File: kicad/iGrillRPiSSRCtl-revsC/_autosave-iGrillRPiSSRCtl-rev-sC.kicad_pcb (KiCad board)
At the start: 2 copper layers, 65 x 56 mm, 21 parts, among them J1 Conn_01x02, P1 Conn_02x20_Odd_Even

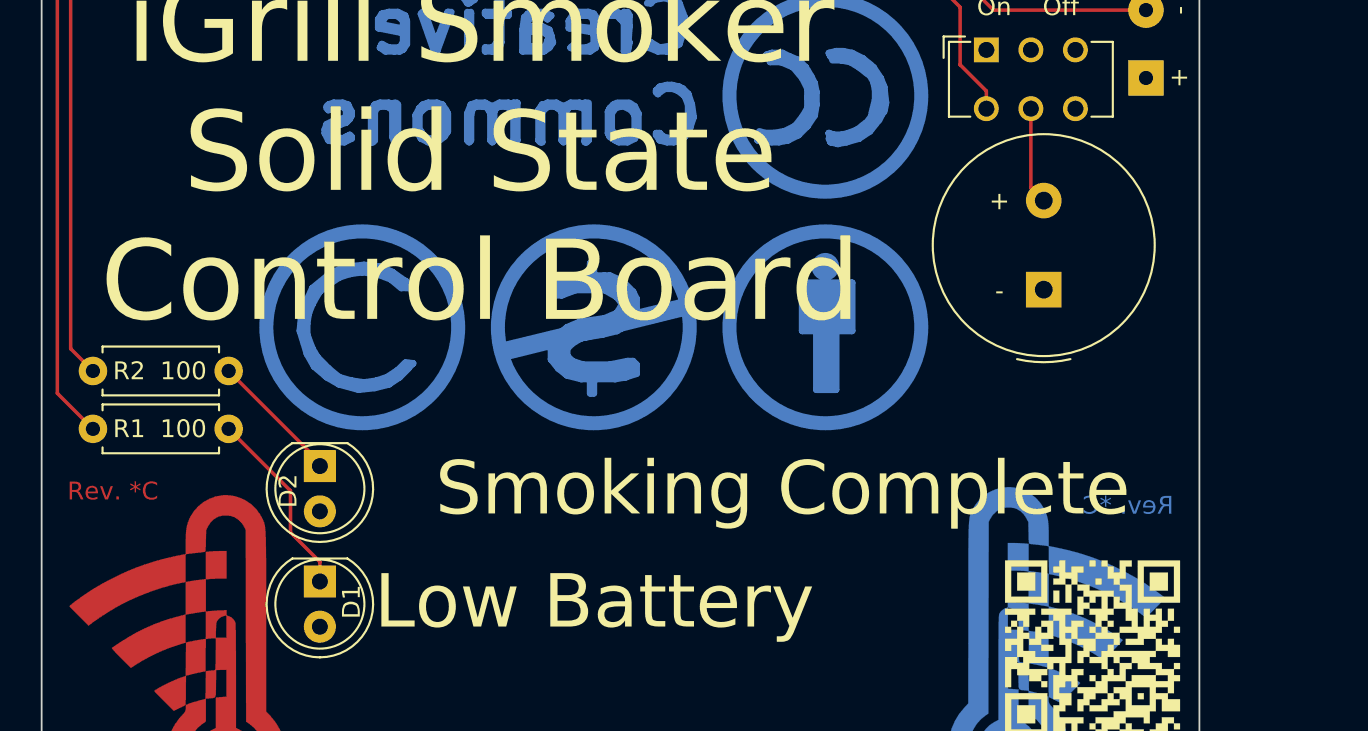
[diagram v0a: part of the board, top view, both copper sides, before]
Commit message: Electrical Cleanup of Schematic
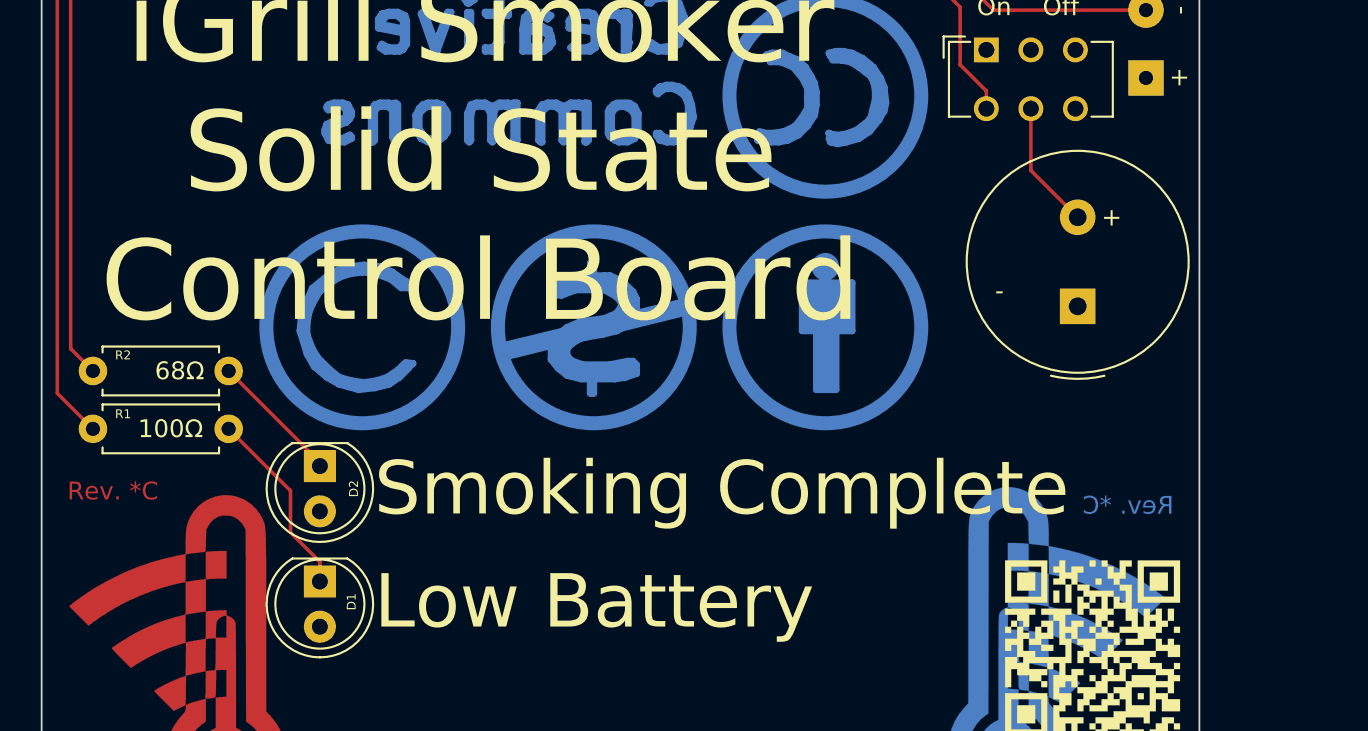
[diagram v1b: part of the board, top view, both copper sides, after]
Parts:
- R1: value 100 -> 100Ω
- R2: value 100 -> 68Ω
- moved BZ1 2.12 mm to (75.3, 43.6)
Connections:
- On    Off pad 6: Net-(SW1-Pad6) -> +5V
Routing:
- net Net-(BZ1-Pad2): track 5.46 -> 7.19 mm
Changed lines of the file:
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@@
     (zones 0)
     (modules 21)
-    (nets 25)
+    (nets 24)
   )
   (page A3)
@@
   (net 22 "Net-(D2-Pad1)")
   (net 23 "Net-(BZ1-Pad2)")
-  (net 24 "Net-(SW1-Pad6)")
   (net_class Default "This is the default net class."
     (clearance 0.2)
@@
     (add_net "Net-(D1-Pad1)")
     (add_net "Net-(D2-Pad1)")
-    (add_net "Net-(SW1-Pad6)")
   )
   (net_class Power ""
@@
     (fp_line (start -1 -0.35) (end -2 0.65) (layer F.Fab) (width 0.1))
     (pad 6 thru_hole circle (at 5 3.3) (size 1.4 1.4) (drill 0.9) (layers *.Cu *.Mask)
-      (net 24 "Net-(SW1-Pad6)"))
+      (net 2 +5V))
     (pad 5 thru_hole circle (at 2.5 3.3) (size 1.4 1.4) (drill 0.9) (layers *.Cu *.Mask)
       (net 23 "Net-(BZ1-Pad2)"))
@@
     (descr "Resistor, Axial_DIN0207 series, Axial, Horizontal, pin pitch=7.62mm, 0.25W = 1/4W, length*diameter=6.3*2.5mm^2, http://cdn-reichelt.de/documents/datenblatt/B400/1_4W%23YAG.pdf")
     (tags "Resistor Axial_DIN0207 series Axial Horizontal pin pitch 7.62mm 0.25W = 1/4W length 6.3mm diameter 2.5mm")
-    (fp_text reference R2 (at 2.032 0) (layer F.SilkS)
-      (effects (font (size 1 1) (thickness 0.15)))
-    )
-    (fp_text value 100 (at 5.08 0) (layer F.SilkS)
+    (fp_text reference R2 (at 1.692 -0.882) (layer F.SilkS)
+      (effects (font (size 0.5 0.5) (thickness 0.075)))
+    )
+    (fp_text value 68Ω (at 4.867 0) (layer F.SilkS)
       (effects (font (size 1 1) (thickness 0.15)))
     )
@@
     (descr "Resistor, Axial_DIN0207 series, Axial, Horizontal, pin pitch=7.62mm, 0.25W = 1/4W, length*diameter=6.3*2.5mm^2, http://cdn-reichelt.de/documents/datenblatt/B400/1_4W%23YAG.pdf")
     (tags "Resistor Axial_DIN0207 series Axial Horizontal pin pitch 7.62mm 0.25W = 1/4W length 6.3mm diameter 2.5mm")
-    (fp_text reference R1 (at 2.032 0) (layer F.SilkS)
-      (effects (font (size 1 1) (thickness 0.15)))
-    )
-    (fp_text value 100 (at 5.08 0) (layer F.SilkS)
+    (fp_text reference R1 (at 1.692 -0.83) (layer F.SilkS)
+      (effects (font (size 0.5 0.5) (thickness 0.075)))
+    )
+    (fp_text value 100Ω (at 4.359 0) (layer F.SilkS)
       (effects (font (size 1 1) (thickness 0.15)))
     )
@@
     (descr "LED, diameter 5.0mm, 2 pins, http://cdn-reichelt.de/documents/datenblatt/A500/LL-504BC2E-009.pdf")
     (tags "LED diameter 5.0mm 2 pins")
-    (fp_text reference D2 (at 1.397 1.778 90) (layer F.SilkS)
-      (effects (font (size 1 1) (thickness 0.15)))
-    )
-    (fp_text value "Smoking Complete" (at 1.27 -45.5 180) (layer F.SilkS)
-      (effects (font (size 3 3) (thickness 0.45)) (justify right))
+    (fp_text reference D2 (at 1.27 -1.905 90) (layer F.SilkS)
+      (effects (font (size 0.5 0.5) (thickness 0.075)))
+    )
+    (fp_text value "Smoking Complete" (at 1.27 -3.048 180) (layer F.SilkS)
+      (effects (font (size 3 3) (thickness 0.45)) (justify left))
     )
     (fp_arc (start 1.27 0) (end -1.29 1.54483) (angle -148.9) (layer F.SilkS) (width 0.12))
@@
     (tags "LED diameter 5.0mm 2 pins")
     (fp_text reference D1 (at 1.143 -1.778 90) (layer F.SilkS)
-      (effects (font (size 1 1) (thickness 0.15)))
+      (effects (font (size 0.5 0.5) (thickness 0.075)))
     )
     (fp_text value "Low Battery" (at 1.143 -3.048 180) (layer F.SilkS)
@@
   )
   (module Buzzer_Beeper:Buzzer_TDK_PS1240P02BT_D12.2mm_H6.5mm (layer F.Cu)
-    (at 73.381 42.685 90)
+    (at 75.286 43.621 90)
     (descr "Buzzer, D12.2mm height 6.5mm, https://product.tdk.com/info/en/catalog/datasheets/piezoelectronic_buzzer_ps_en.pdf")
     (tags buzzer)
@@
     (effects (font (size 1 1) (thickness 0.15)))
   )
-  (gr_text + (at 70.8918 37.7066) (layer F.SilkS)
+  (gr_text + (at 77.191 38.621) (layer F.SilkS)
     (effects (font (size 1 1) (thickness 0.15)))
   )
@@
   (segment (start 32.741 52.371) (end 32.741 52.591) (width 0.2) (layer F.Cu) (net 22))
   (segment (start 27.62 47.25) (end 32.741 52.371) (width 0.2) (layer F.Cu) (net 22))
-  (segment (start 72.659 36.963) (end 73.381 37.685) (width 0.2) (layer F.Cu) (net 23))
-  (segment (start 72.659 32.523) (end 72.659 36.963) (width 0.2) (layer F.Cu) (net 23))
+  (segment (start 72.659 35.994) (end 75.286 38.621) (width 0.2) (layer F.Cu) (net 23))
+  (segment (start 72.659 32.523) (end 72.659 35.994) (width 0.2) (layer F.Cu) (net 23))
   (zone (net 2) (net_name +5V) (layer F.Cu) (hatch edge 0.508)
     (connect_pads (clearance 0.508))
